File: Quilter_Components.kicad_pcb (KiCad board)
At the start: 4 copper layers, 40.4 x 100 mm, 138 parts, among them J1 Conn_01x10_Male, J2 Conn_01x10_Male, J3 Conn_01x10_Male, J4 Eurorack_10_pin_power, U1 TL072, U10 SSI2144, U2 TL074, U3 TL074, U4 TL074, U5 SSI2144, U7 SSI2144, U9 SSI2144

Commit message: Draft of 8HP component PCB routed
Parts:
- moved C28 137.1 mm to (52.6, 123.8), turned to -90 degrees
- moved C24 135.1 mm to (54.2, 123.8), turned to -90 degrees
- moved C25 133.2 mm to (55.8, 123.8), turned to -90 degrees
- moved C21 131.3 mm to (57.4, 123.8), turned to 90 degrees
- moved R43 129.4 mm to (59.0, 123.8), turned to 90 degrees
- moved U9 129.0 mm to (55.3, 130.5), turned to -90 degrees
- moved C23 128.4 mm to (52.6, 137.2), turned to 90 degrees
- moved R42 127.5 mm to (60.6, 123.8), turned to -90 degrees
- moved C22 126.3 mm to (54.2, 137.2), turned to 90 degrees
- moved R41 125.6 mm to (62.2, 123.8), turned to 90 degrees
- moved V_OCT4 125.0 mm to (66.5, 117.3), turned to 180 degrees
- moved R53 124.3 mm to (55.8, 137.2), turned to 90 degrees
- moved C26 123.8 mm to (63.8, 123.8), turned to 90 degrees
- moved R52 122.2 mm to (57.4, 137.2), turned to 90 degrees
- moved R51 121.9 mm to (65.4, 123.8), turned to 90 degrees
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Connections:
- J1 pad 3: unconnected-(J1-Pad3) -> /AUDIO_BUFF3
- J1 pad 7: unconnected-(J1-Pad7) -> /FREQ_V_OCT2
- J1 pad 8: /AUDIO_BUFF4 -> unconnected-(J1-Pad8)
- J2 pad 2: /AUDIO_BUFF3 -> unconnected-(J2-Pad2)
- J2 pad 4: /FREQ_V_OCT2 -> unconnected-(J2-Pad4)
- J2 pad 5: unconnected-(J2-Pad5) -> /AUDIO_BUFF4
- J3 pad 1: unconnected-(J3-Pad1) -> /AUDIO_IN4
- J3 pad 3: /FREQ_CV4 -> unconnected-(J3-Pad3)
- J3 pad 5: /AUDIO_IN4 -> /FREQ_POT
- J3 pad 6: /FREQ_CV1 -> /FREQ_CV4
- J3 pad 7: /FREQ_POT -> /FREQ_CV1
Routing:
- net -12V: track 52.6 -> 235.2 mm, vias 2 -> 8
- net +12V: track 45.0 -> 204.8 mm, vias 2 -> 11
- net /Q_POT: track 0.00 -> 157.4 mm
- net /FREQ_POT: track 0.00 -> 83.5 mm, vias 0 -> 3
- net /Audio_Out4: track 15.4 -> 72.6 mm, vias 0 -> 2
- net /Audio_Out3: track 15.6 -> 69.1 mm, vias 0 -> 2
- net /FREQ_CV1: track 0.00 -> 42.3 mm, vias 0 -> 1
- net /FREQ_V_OCT1: track 0.00 -> 39.1 mm, vias 0 -> 1
- net /Audio_Out1: track 5.79 -> 41.7 mm, vias 0 -> 2
- net /FREQ_CV2: track 0.00 -> 33.5 mm, vias 0 -> 1
- net /AUDIO_IN2: track 0.00 -> 31.1 mm, vias 0 -> 1
- net /FREQ_V_OCT4: track 0.00 -> 29.9 mm, vias 0 -> 1
- net /FREQ_CV4: track 0.00 -> 28.6 mm, vias 0 -> 1
- net /AUDIO_IN3: track 0.00 -> 28.4 mm, vias 0 -> 1
- net /Audio_Out2: track 22.6 -> 44.0 mm, vias 0 -> 2
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
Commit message: First draft routing of Controls PCB
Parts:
- moved J2 0.24 mm to (87.9, 62.8)
- moved J1 0.16 mm to (52.4, 62.8)
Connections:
- J1 pad 1: unconnected-(J1-Pad1) -> -12V
- J2 pad 1: unconnected-(J2-Pad1) -> +12V
- J2 pad 10: /FREQ_POT_5V -> /AUDIO_IN2
- J2 pad 7: unconnected-(J2-Pad7) -> /FREQ_POT_5V
- J2 pad 9: /AUDIO_IN2 -> unconnected-(J2-Pad9)
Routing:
- net -12V: track 235.2 -> 240.4 mm
- net +12V: track 204.8 -> 209.5 mm
- net /FREQ_POT_5V: track 15.4 -> 11.4 mm
- net /FREQ_CV2: track 33.5 -> 30.2 mm
- net /AUDIO_IN2: track 31.1 -> 28.6 mm

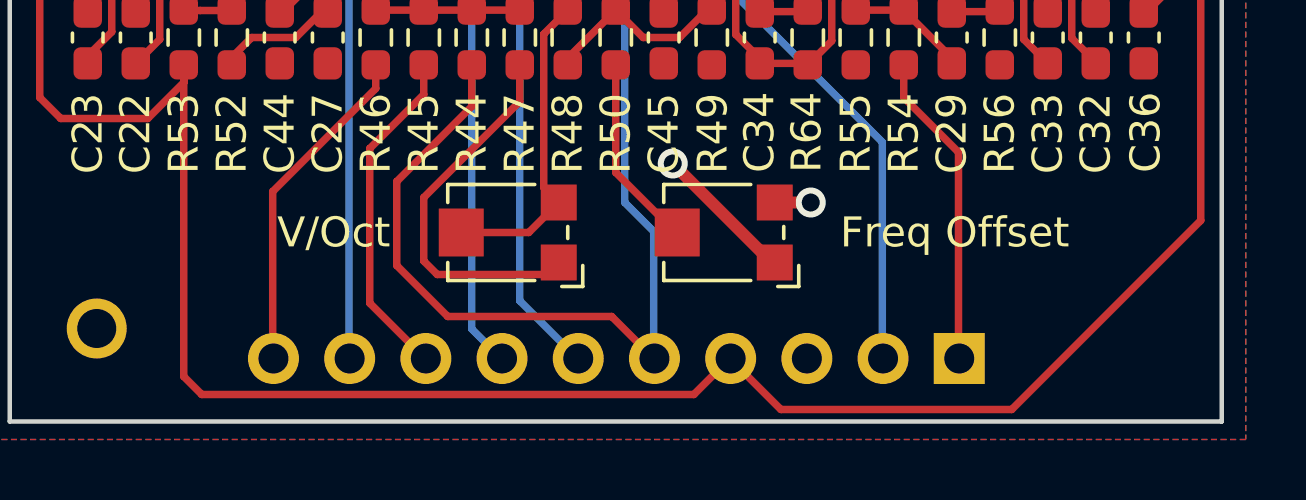
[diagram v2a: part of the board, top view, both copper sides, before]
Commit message: Fixed orientation of connector headers
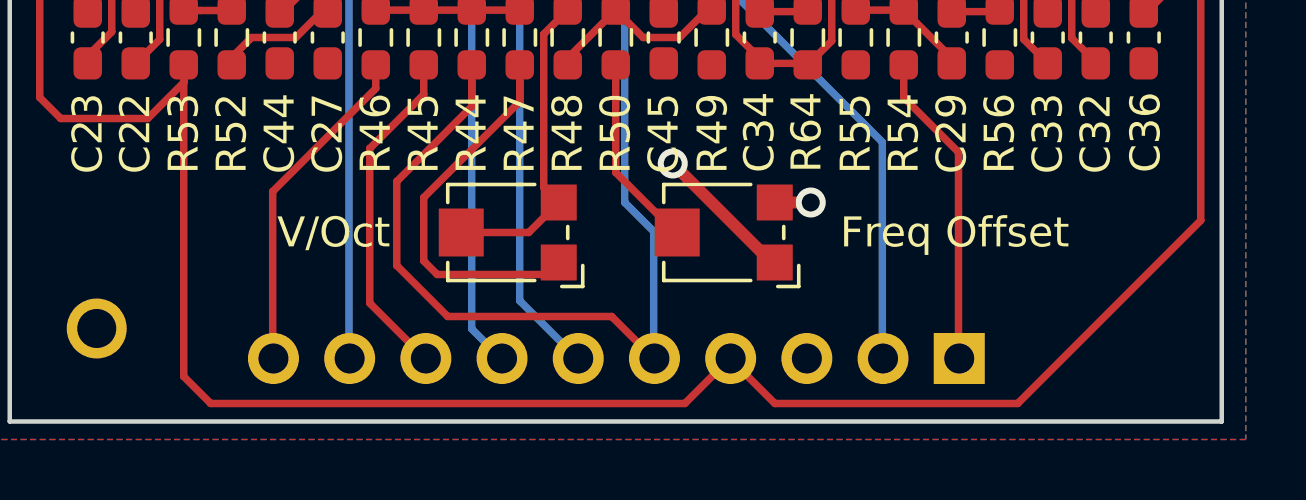
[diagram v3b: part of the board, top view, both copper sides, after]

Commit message: Reorganisation of component board
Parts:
- moved FREQ_OFFSET2 27.6 mm to (84.0, 110.8)
- moved V_OCT3 26.6 mm to (56.4, 119.1), turned to 0 degrees
- moved R56 26.4 mm to (56.7, 134.4), turned to 180 degrees
- moved R30 26.3 mm to (56.7, 104.9), turned to 180 degrees
- moved FREQ_OFFSET4 25.2 mm to (84.0, 140.3)
- moved C20 25.2 mm to (63.5, 111.7), turned to 0 degrees
- moved C28 25.0 mm to (76.9, 117.9), turned to 180 degrees
- moved R17 24.7 mm to (83.6, 93.7), turned to 0 degrees
- moved C36 24.6 mm to (63.5, 141.2), turned to 0 degrees
- moved R43 24.6 mm to (83.6, 123.2), turned to 0 degrees
- moved C12 24.5 mm to (76.9, 88.4), turned to 180 degrees
- moved V_OCT1 24.2 mm to (56.4, 89.6), turned to 0 degrees
- moved C16 23.2 mm to (63.5, 109.9), turned to 180 degrees
- moved R28 23.1 mm to (56.7, 106.5), turned to 180 degrees
- moved R54 23.1 mm to (56.7, 136.0), turned to 180 degrees
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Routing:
- net /Q_POT: track 157.5 -> 0.00 mm
- net /FREQ_POT: track 83.5 -> 0.00 mm, vias 3 -> 0
- net /Audio_Out4: track 72.6 -> 15.7 mm, vias 2 -> 1
- net /Audio_Out3: track 69.1 -> 18.7 mm, vias 2 -> 1
- net -12V: track 240.4 -> 198.0 mm, vias 8 -> 2
- net /FREQ_CV1: track 42.3 -> 0.00 mm, vias 1 -> 0
- net /FREQ_V_OCT4: track 29.9 -> 0.00 mm, vias 1 -> 0
- net /FREQ_CV4: track 28.6 -> 0.00 mm, vias 1 -> 0
- net /AUDIO_IN3: track 28.4 -> 0.00 mm, vias 1 -> 0
- net /AUDIO_IN2: track 28.6 -> 2.30 mm, vias 1 -> 0
- net /Audio_Out2: track 44.0 -> 21.8 mm, vias 2 -> 1
- net /FREQ_V_OCT1: track 39.1 -> 19.0 mm, vias 1 -> 0
- net /FREQ_V_OCT2: track 20.0 -> 0.00 mm
- net Net-(R35-Pad2): track 18.9 -> 38.2 mm
- net Net-(R61-Pad2): track 19.5 -> 38.7 mm
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
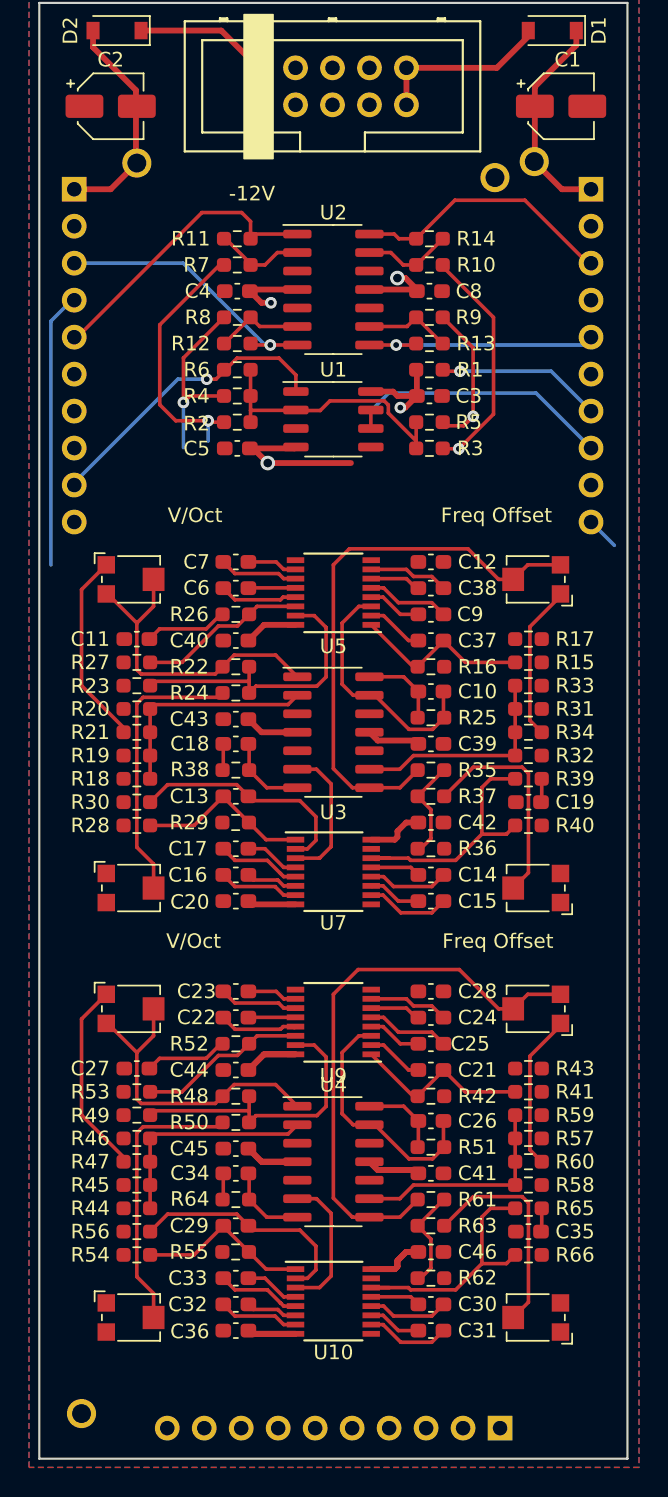
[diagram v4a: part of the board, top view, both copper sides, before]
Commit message: Re-routed Controls board
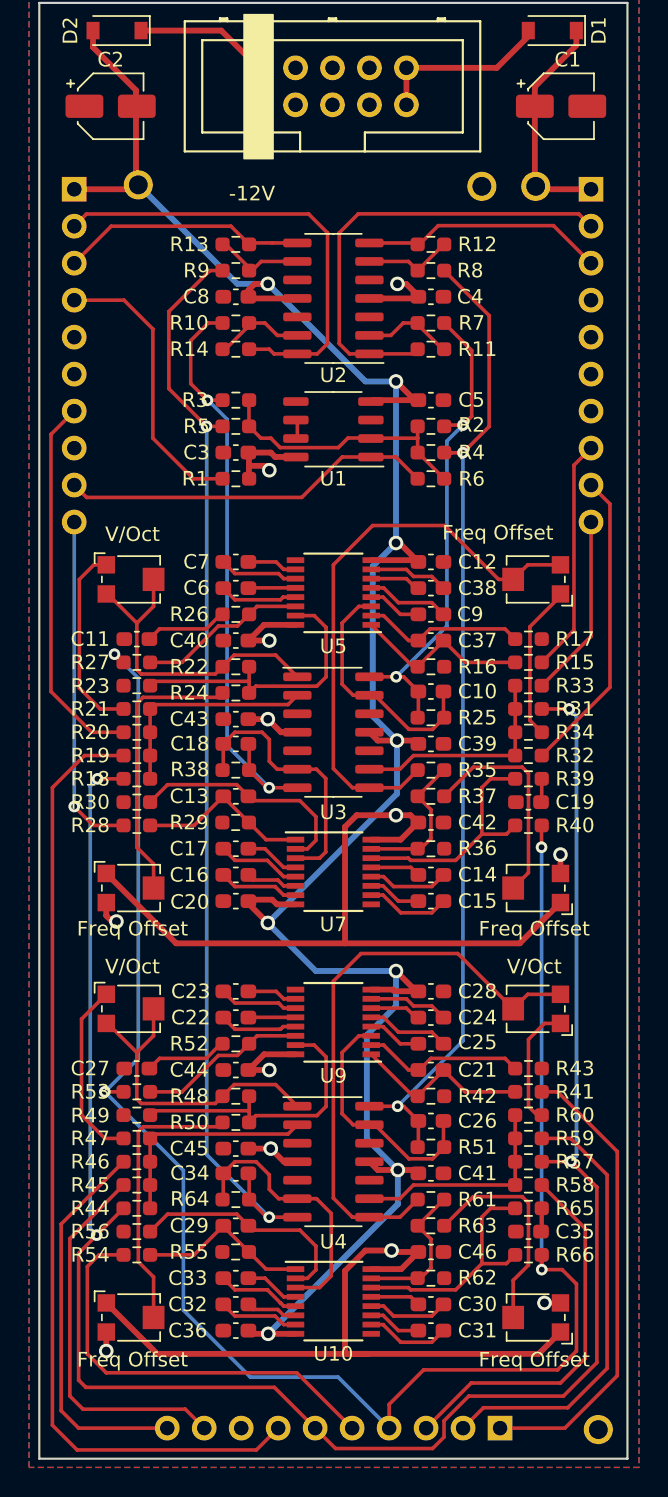
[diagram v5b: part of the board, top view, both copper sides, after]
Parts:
- moved TP3 35.5 mm to (88.4, 148.0)
- moved R11 15.3 mm to (76.9, 73.8), turned to 0 degrees
- moved R14 15.3 mm to (63.5, 73.8), turned to 180 degrees
- moved R6 15.3 mm to (76.9, 82.7)
- moved R1 15.3 mm to (63.5, 82.7), turned to 180 degrees
- moved R12 14.9 mm to (76.9, 66.6), turned to 0 degrees
- moved R13 14.9 mm to (63.5, 66.6), turned to 180 degrees
- moved R7 13.9 mm to (76.9, 72.0), turned to 0 degrees
- moved R10 13.9 mm to (63.5, 72.0), turned to 180 degrees
- moved R4 13.9 mm to (76.9, 80.9), turned to 0 degrees
- moved C3 13.9 mm to (63.5, 80.9), turned to 180 degrees
- moved C5 13.7 mm to (76.9, 77.3), turned to 0 degrees
- moved R3 13.7 mm to (63.5, 77.3), turned to 180 degrees
- moved R8 13.7 mm to (76.9, 68.4), turned to 0 degrees
- moved R9 13.7 mm to (63.5, 68.4), turned to 180 degrees
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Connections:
- J1 pad 10: /AUDIO_IN1 -> /AUDIO_IN2
- J1 pad 2: unconnected-(J1-Pad2) -> /AUDIO_BUFF2
- J1 pad 3: /AUDIO_BUFF3 -> /AUDIO_BUFF4
- J1 pad 4: /FREQ_V_OCT1 -> /FREQ_POT_5V
- J1 pad 5: /AUDIO_BUFF1 -> unconnected-(J1-Pad5)
- J1 pad 7: /FREQ_V_OCT2 -> /FREQ_V_OCT1
- J2 pad 10: /AUDIO_IN2 -> /FREQ_V_OCT2
- J2 pad 2: unconnected-(J2-Pad2) -> /AUDIO_BUFF1
- J2 pad 3: /AUDIO_BUFF2 -> /AUDIO_BUFF3
- J2 pad 5: /AUDIO_BUFF4 -> unconnected-(J2-Pad5)
- J2 pad 7: /FREQ_POT_5V -> unconnected-(J2-Pad7)
- J2 pad 8: /FREQ_CV2 -> /AUDIO_IN1
- J2 pad 9: unconnected-(J2-Pad9) -> /FREQ_CV2
- J3 pad 1: /AUDIO_IN4 -> /AUDIO_IN3
- J3 pad 3: unconnected-(J3-Pad3) -> /FREQ_CV4
- J3 pad 5: /FREQ_POT -> /AUDIO_IN4
- J3 pad 6: /FREQ_CV4 -> /FREQ_POT
- J3 pad 8: /FREQ_CV3 -> unconnected-(J3-Pad8)
- J3 pad 9: /AUDIO_IN3 -> /FREQ_CV3
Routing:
- net /FREQ_POT: track 0.00 -> 137.2 mm, vias 0 -> 4
- net /Q_POT: track 0.00 -> 123.5 mm, vias 0 -> 4
- net /FREQ_CV1: track 0.00 -> 66.4 mm
- net /Audio_Out4: track 15.7 -> 77.1 mm, vias 1 -> 2
- net /Audio_Out3: track 18.7 -> 68.2 mm, vias 1 -> 2
- net +12V: track 196.4 -> 241.7 mm, vias 2 -> 8
- net /AUDIO_IN3: track 0.00 -> 31.8 mm
- net /FREQ_V_OCT4: track 0.00 -> 30.4 mm
- net /AUDIO_IN4: track 0.00 -> 29.1 mm
- net /FREQ_V_OCT3: track 0.23 -> 26.7 mm
- net /FREQ_CV3: track 0.00 -> 26.2 mm
- net /FREQ_CV4: track 0.00 -> 26.1 mm
- net /AUDIO_IN2: track 2.30 -> 23.5 mm, vias 0 -> 1
- net /Audio_Out2: track 21.8 -> 42.8 mm, vias 1 -> 2
- net -12V: track 198.0 -> 215.8 mm, vias 2 -> 12
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
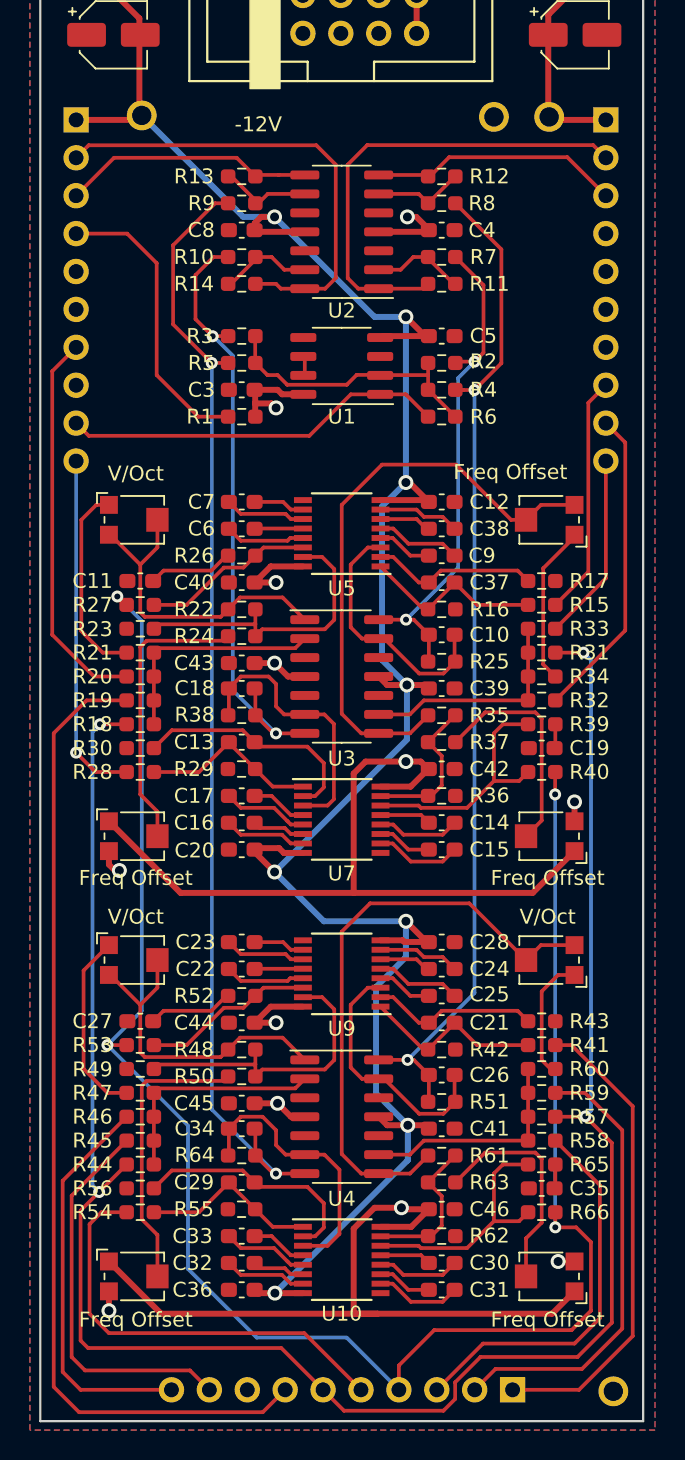
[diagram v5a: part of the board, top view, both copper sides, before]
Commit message: Added all voice filter CV; panel draft done
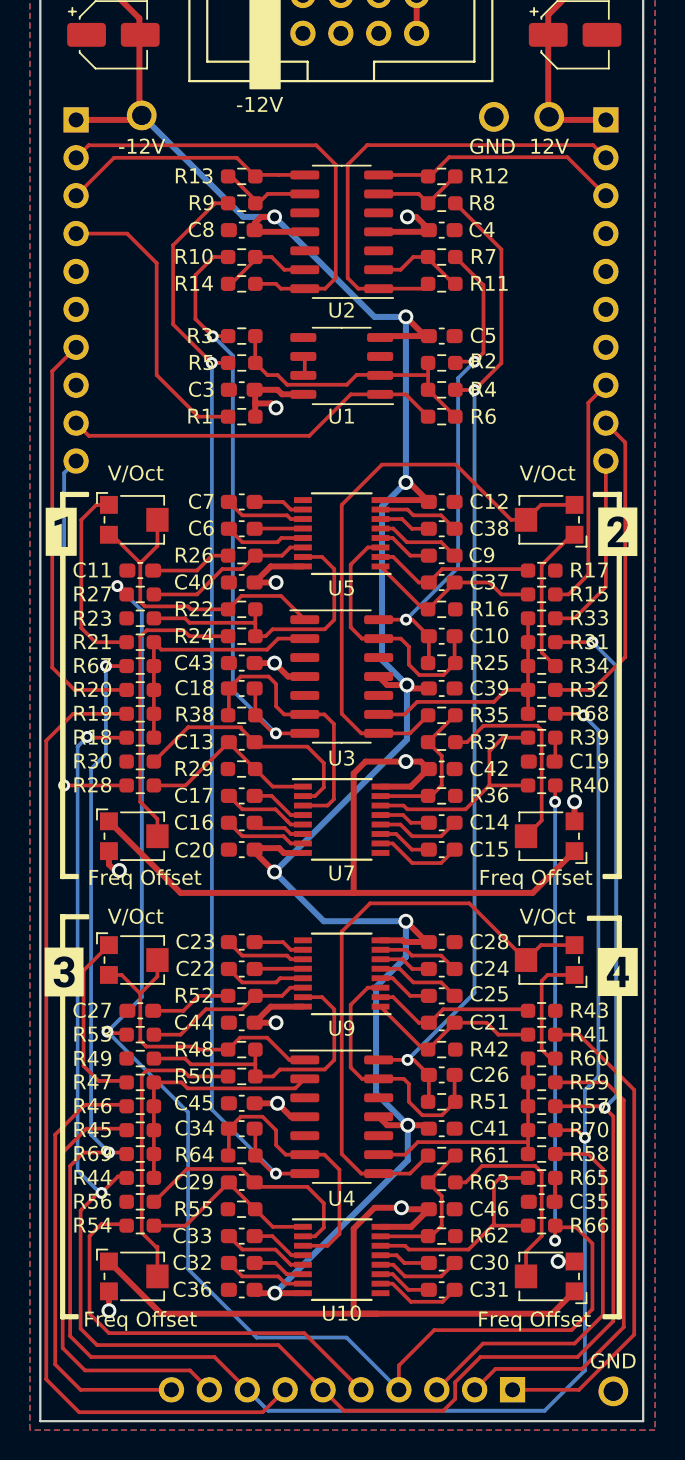
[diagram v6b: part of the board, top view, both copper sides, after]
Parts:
- added R67: 100k, Resistor_SMD:R_0603_1608Metric_Pad0.98x0.95mm_HandSolder, F.Cu at (56.7, 99.4)
- added R68: 100k, Resistor_SMD:R_0603_1608Metric_Pad0.98x0.95mm_HandSolder, F.Cu at (83.6, 102.6)
- added R69: 100k, Resistor_SMD:R_0603_1608Metric_Pad0.98x0.95mm_HandSolder, F.Cu at (56.7, 132.1)
- added R70: 100k, Resistor_SMD:R_0603_1608Metric_Pad0.98x0.95mm_HandSolder, F.Cu at (83.6, 130.5)
- added kibuzzard-63F9EABE: G***, kibuzzard-63F9EABE, F.Cu at (51.4, 90.4)
- added kibuzzard-63F9EC4B: G***, kibuzzard-63F9EC4B, F.Cu at (51.6, 119.9)
- added kibuzzard-63F9EC99: G***, kibuzzard-63F9EC99, F.Cu at (88.7, 90.4)
- added kibuzzard-63F9ECEE: G***, kibuzzard-63F9ECEE, F.Cu at (88.7, 119.9)
- moved C35 0.90 mm to (83.6, 135.3)
- moved R18 0.90 mm to (56.7, 104.2)
- moved R20 0.90 mm to (56.7, 101.0)
- moved R28 0.90 mm to (56.7, 107.4)
- moved R39 0.90 mm to (83.6, 104.2)
- moved R40 0.90 mm to (83.6, 107.4)
- moved R54 0.90 mm to (56.7, 136.9)
- moved R56 0.90 mm to (56.7, 135.3)
- moved R58 0.90 mm to (83.6, 132.1)
- moved R66 0.90 mm to (83.6, 136.9)
- moved C19 0.90 mm to (83.6, 105.8)
- moved R19 0.90 mm to (56.7, 102.6)
- moved R30 0.90 mm to (56.7, 105.8)
- moved R44 0.90 mm to (56.7, 133.7)
- moved R65 0.90 mm to (83.6, 133.7)
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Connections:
- J3 pad 8: unconnected-(J3-Pad8) -> /FREQ_JACK
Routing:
- net /FREQ_JACK: track 0.00 -> 137.0 mm, vias 0 -> 4
- net /FREQ_CV3: track 26.2 -> 29.0 mm
- net /FREQ_V_OCT3: track 26.7 -> 29.5 mm
- net /AUDIO_IN2: track 23.5 -> 26.3 mm
- net /FREQ_POT: track 137.2 -> 139.5 mm
- net Net-(R32-Pad1): track 15.2 -> 17.1 mm
- net Net-(R19-Pad1): track 15.3 -> 17.0 mm
- net /FREQ_V_OCT1: track 26.1 -> 27.7 mm
- net /FREQ_V_OCT4: track 30.4 -> 32.0 mm
- net Net-(R58-Pad1): track 15.2 -> 16.8 mm
- net Net-(R45-Pad1): track 15.3 -> 16.8 mm
- net Net-(FREQ_OFFSET4-Pad2): track 15.1 -> 13.8 mm
- net Net-(FREQ_OFFSET2-Pad2): track 15.1 -> 13.9 mm
- net Net-(R48-Pad2): track 21.9 -> 20.7 mm
- net /AUDIO_IN3: track 31.8 -> 32.9 mm
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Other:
- board text added: "-12V"
- board text added: "12V"
- board text added: "GND"
